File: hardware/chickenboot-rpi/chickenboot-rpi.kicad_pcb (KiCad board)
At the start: 2 copper layers, 33.5 x 18 mm, 40 parts, among them J1 USB_C_Receptacle_USB2.0, J2 Conn_01x03, J3 Conn_01x03, J4 JTAG, Q1 LP0404N3T5G, SW1 SW_Push, SW2 SW_Push, U1 RP2350_60QFN, U2 HT7533-1, U3 USBLC6-2P6, Y1 12MHz

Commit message: clean schematics and version match between schematics and PCB
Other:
- board text added: "JTAG v0.1"
- board text removed: "JTAG v0.09"
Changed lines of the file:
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@@
 		)
 		(property "Value" "12MHz"
-			(at 0 4.55 360)
+			(at 0 4.55 0)
 			(layer "F.Fab")
 			(effects
@@
 		)
 		(property "LCSC Part" "C5830660"
-			(at 0 0 360)
+			(at 0 0 0)
 			(layer "F.Fab")
 			(hide yes)
@@
 		)
 		(fp_text user "${REFERENCE}"
-			(at 0 0 360)
+			(at 0 0 0)
 			(layer "F.Fab")
 			(effects
@@
 		)
 	)
-	(gr_text "JTAG v0.09"
+	(gr_text "JTAG v0.1"
 		(at 130.4 117.48 0)
 		(layer "B.Mask")

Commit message: add BOM/POS for manufacturing and related fixes
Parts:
- removed C10, C9: 4.7u, Capacitor_SMD:C_0402_1005Metric
- removed C7: 4.7u, RP2350_60QFN_minimal:C_0402_1005Metric_small_pads
- removed J4: JTAG, Connector_IDC:IDC-Header_2x03_P2.54mm_Vertical
- removed Q1: LP0404N3T5G, Package_TO_SOT_SMD:SOT-883
- added C3: 4.7u, RP2350_60QFN_minimal:C_0402_1005Metric_small_pads, F.Cu at (115.2, 102.4)
- added C4: 4.7u 10V, RP2350_60QFN_minimal:C_0402_1005Metric_small_pads, F.Cu at (114.8, 104.6)
- added C5: 4.7u, RP2350_60QFN_minimal:C_0402_1005Metric_small_pads, F.Cu at (125.8, 105.8)
- added CN1: 69168-106HLF, easyeda2kicad:CONN-TH_6P-P2.54_69168-X06, F.Cu at (131.7, 109.7)
- added Q2: WPM2093-3/TR, easyeda2kicad:SOT-723_L1.2-W0.8-P0.80-LS1.2-BR, F.Cu at (123.3, 101.5)
- C6: value 4.7u -> 4.7u 10V
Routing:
- net TARGET_VCC: track 9.98 -> 11.7 mm
- net +3V3: track 38.9 -> 37.2 mm, vias 2 -> 0

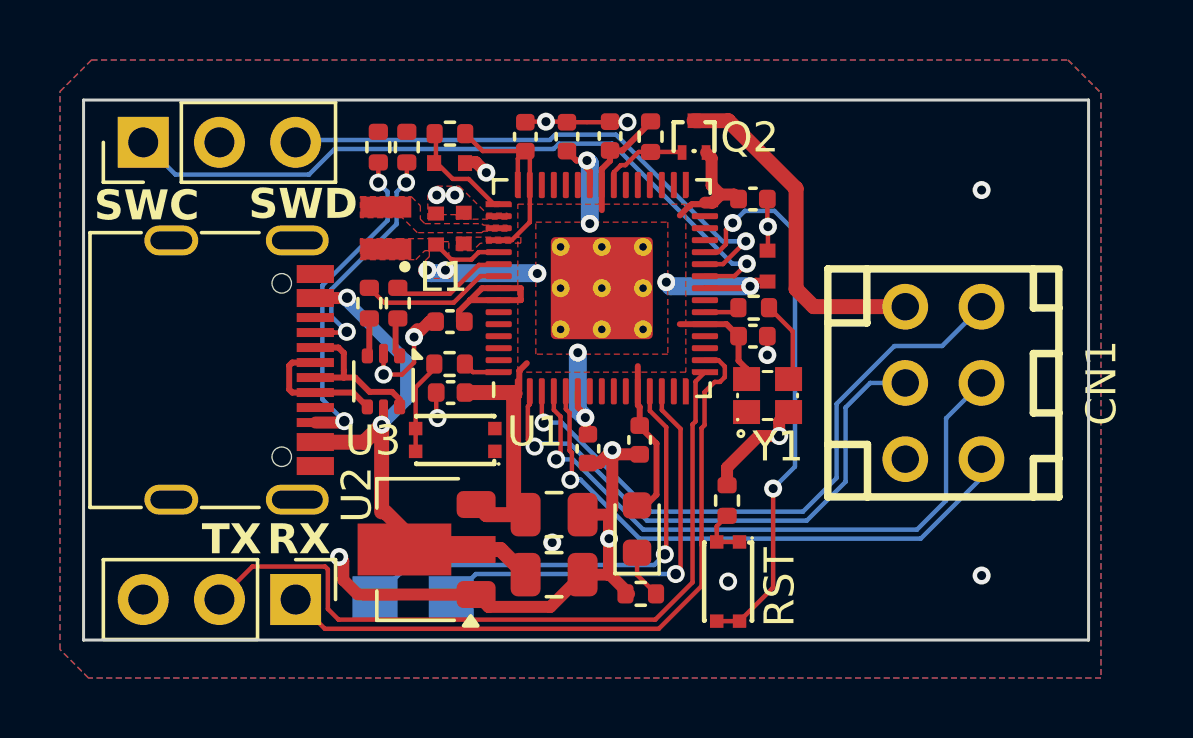
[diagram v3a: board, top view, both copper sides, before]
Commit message: change boards shape and fixes for manufacturability
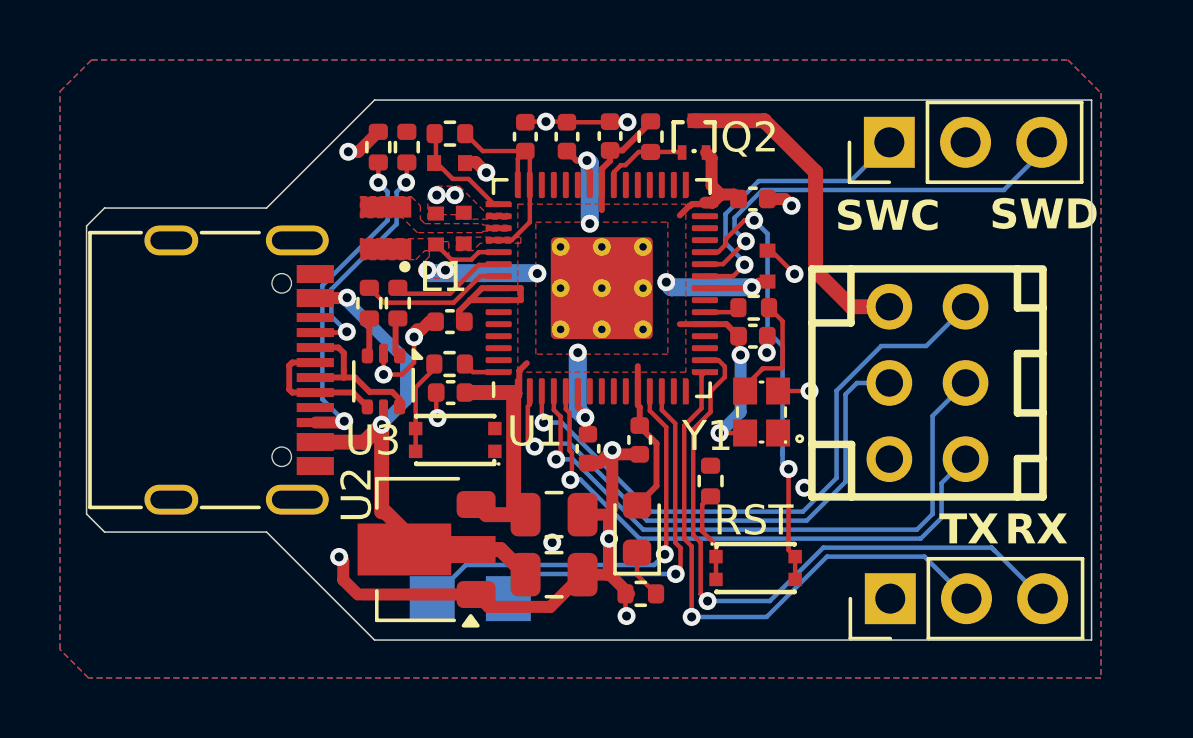
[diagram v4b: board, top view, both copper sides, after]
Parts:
- moved J2 24.9 mm to (129.9, 101.7)
- moved J3 19.8 mm to (129.9, 116.9), turned to 90 degrees
- moved TP1 1.91 mm to (114.6, 116.9)
- moved TP2 1.91 mm to (117.2, 116.9)
- moved SW2 1.02 mm to (125.4, 115.9), turned to 0 degrees
- moved R1 0.85 mm to (123.9, 113.0)
- moved Y1 0.59 mm to (125.6, 110.7), turned to 90 degrees
- moved CN1 0.53 mm to (131.1, 109.7)
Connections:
- J3 pad 1: RX -> GND
- J3 pad 3: GND -> RX
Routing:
- net /SWCLK: track 24.3 -> 9.88 mm
- net TX: track 25.4 -> 19.1 mm, vias 0 -> 1
- net /SWD: track 18.3 -> 14.1 mm
- net /RUN: track 18.7 -> 14.8 mm
- net +3V3: track 37.2 -> 40.2 mm, vias 0 -> 2
- net /GPIO9: track 14.2 -> 12.3 mm
- net /GPIO8: track 16.0 -> 14.0 mm
- net Net-(R1-Pad1): track 1.77 -> 3.07 mm
- net RX: track 23.2 -> 22.0 mm, vias 0 -> 1
- net Net-(R9-Pad2): track 2.76 -> 3.92 mm
- net TARGET_VCC: track 11.7 -> 11.0 mm
- net GND: track 33.2 -> 33.0 mm, vias 18 -> 19
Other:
- outline, holes or cut-outs redrawn

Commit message: add status led and use all 27R instead of 33R to optimize components
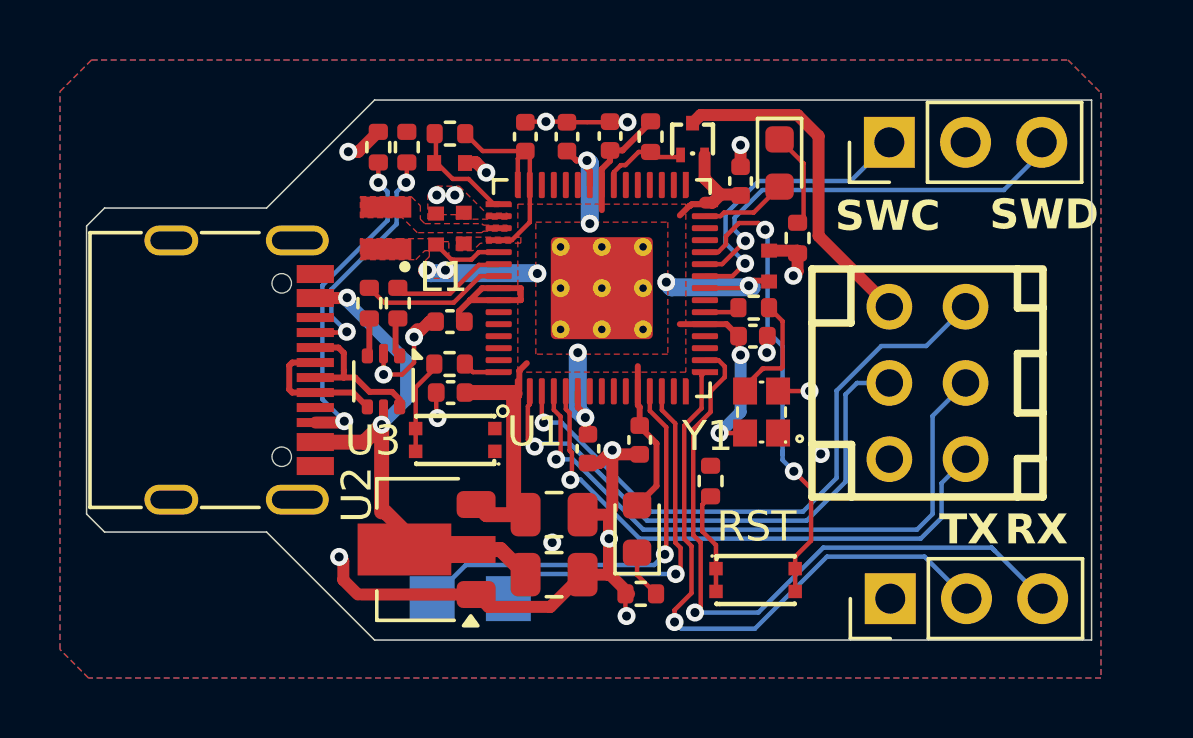
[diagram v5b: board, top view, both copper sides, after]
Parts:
- added LED2: YELLOW, LED_SMD:LED_0603_1608Metric, F.Cu at (126.2, 102.4)
- added R11: 5.1K 1%, Resistor_SMD:R_0402_1005Metric, F.Cu at (126.8, 104.9)
- R5, R9: value 33 -> 27
- moved C16 0.73 mm to (124.9, 103.0), turned to 90 degrees
- moved SW2 0.40 mm to (125.4, 116.3)
- moved Q2 0.09 mm to (123.3, 101.6)
- turned R5 to 0 degrees
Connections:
- R5 pad 1: +3V3 -> /VREG_AVDD
- R5 pad 2: /VREG_AVDD -> +3V3
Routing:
- net Net-(LED2-K): track 0.00 -> 3.19 mm
- net /GPIO18: track 0.00 -> 2.89 mm
- net TX: track 19.1 -> 20.3 mm
- net RX: track 22.0 -> 22.9 mm
- net /RUN: track 14.8 -> 15.7 mm
